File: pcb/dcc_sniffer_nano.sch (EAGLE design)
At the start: 8 parts, among them X1 RT034 Typ 086

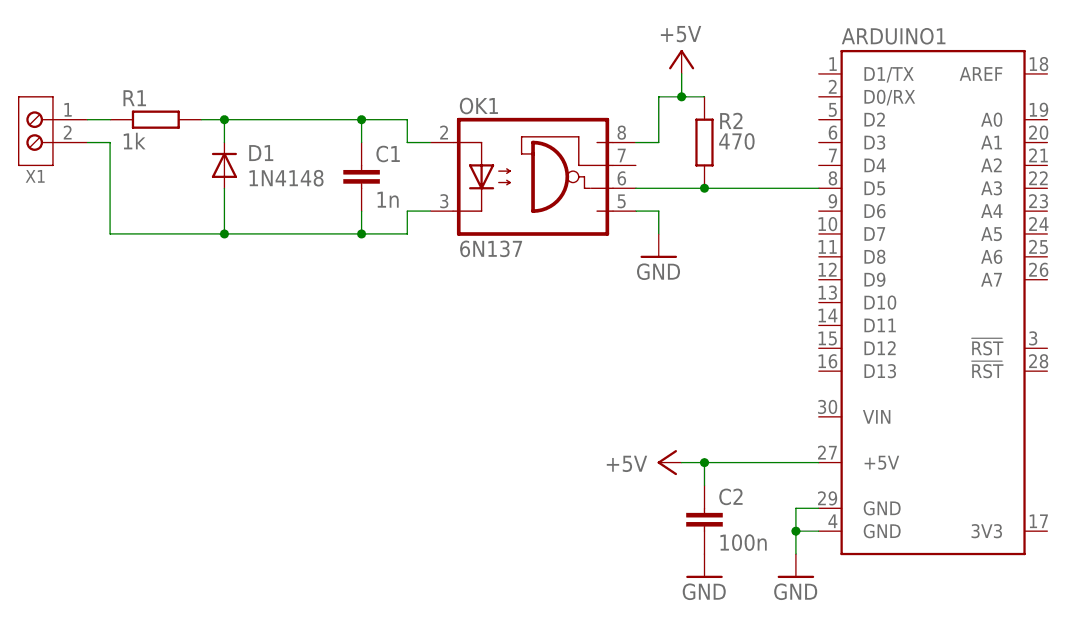
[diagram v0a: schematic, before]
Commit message: bugfix: assign to IRQ input pin
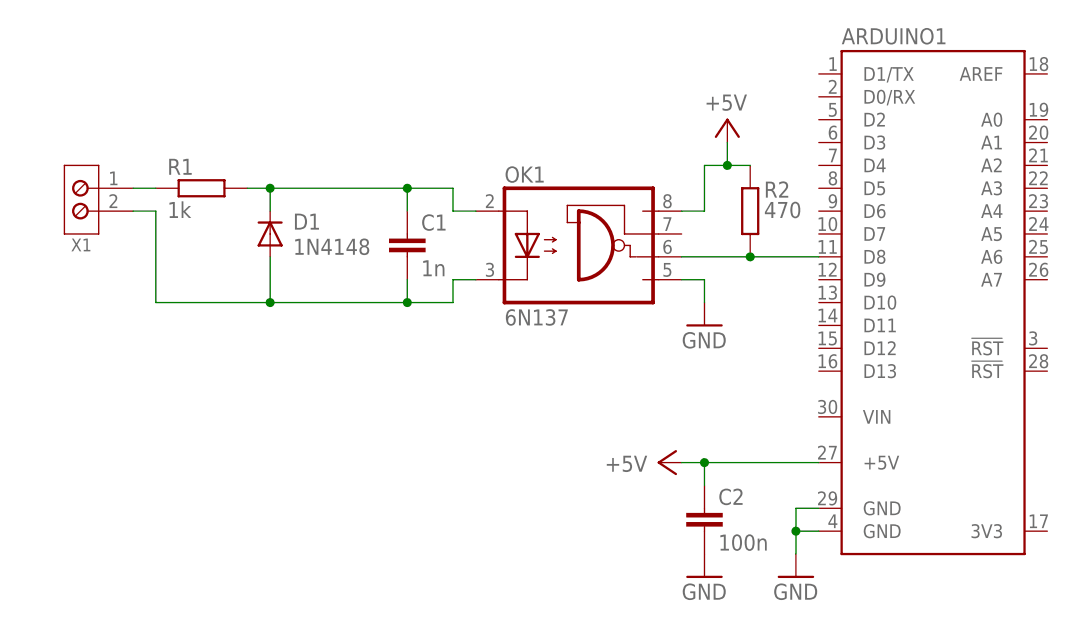
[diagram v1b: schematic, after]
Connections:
- net N$3: now also ARDUINO1.D8; no longer ARDUINO1.D5
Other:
- moved on the sheet: C1, D1, OK1, R1, R2, X1
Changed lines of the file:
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@@
 <sheet>
 <plain>
-<wire x1="30.48" y1="109.22" x2="34.29" y2="109.22" width="0.1524" layer="94"/>
-<wire x1="34.29" y1="109.22" x2="34.29" y2="116.84" width="0.1524" layer="94"/>
-<wire x1="34.29" y1="116.84" x2="30.48" y2="116.84" width="0.1524" layer="94"/>
-<wire x1="30.48" y1="116.84" x2="30.48" y2="109.22" width="0.1524" layer="94"/>
-<text x="29.718" y="108.458" size="1.4224" layer="98" font="vector" ratio="15" rot="R90">to track</text>
+<wire x1="35.56" y1="101.6" x2="39.37" y2="101.6" width="0.1524" layer="94"/>
+<wire x1="39.37" y1="101.6" x2="39.37" y2="109.22" width="0.1524" layer="94"/>
+<wire x1="39.37" y1="109.22" x2="35.56" y2="109.22" width="0.1524" layer="94"/>
+<wire x1="35.56" y1="109.22" x2="35.56" y2="101.6" width="0.1524" layer="94"/>
+<text x="34.798" y="100.838" size="1.4224" layer="98" font="vector" ratio="15" rot="R90">to track</text>
 </plain>
 <instances>
 <instance part="FRAME1" gate="G$1" x="0" y="0"/>
 <instance part="GND1" gate="1" x="116.84" y="63.5"/>
-<instance part="OK1" gate="A" x="88.9" y="106.68"/>
-<instance part="X1" gate="G$1" x="33.02" y="114.3" smashed="yes">
-<attribute name="PART" x="33.528" y="108.712" size="1.4224" layer="95" rot="R180"/>
+<instance part="OK1" gate="A" x="93.98" y="99.06"/>
+<instance part="X1" gate="G$1" x="38.1" y="106.68" smashed="yes">
+<attribute name="PART" x="38.608" y="101.092" size="1.4224" layer="95" rot="R180"/>
 </instance>
-<instance part="X1" gate="G$2" x="33.02" y="111.76" smashed="yes"/>
+<instance part="X1" gate="G$2" x="38.1" y="104.14" smashed="yes"/>
 <instance part="P+1" gate="1" x="101.6" y="76.2" smashed="yes" rot="R90">
 <attribute name="VALUE" x="100.33" y="76.962" size="1.778" layer="96" rot="R180"/>
 </instance>
-<instance part="D1" gate="G$1" x="53.34" y="109.22" smashed="yes" rot="R90">
-<attribute name="NAME" x="55.88" y="109.7026" size="1.778" layer="95"/>
-<attribute name="VALUE" x="55.88" y="106.9086" size="1.778" layer="96"/>
+<instance part="D1" gate="G$1" x="58.42" y="101.6" smashed="yes" rot="R90">
+<attribute name="NAME" x="60.96" y="102.0826" size="1.778" layer="95"/>
+<attribute name="VALUE" x="60.96" y="99.2886" size="1.778" layer="96"/>
 </instance>
-<instance part="R1" gate="G$1" x="45.72" y="114.3"/>
-<instance part="GND2" gate="1" x="101.6" y="99.06"/>
-<instance part="P+2" gate="1" x="104.14" y="121.92" smashed="yes">
-<attribute name="VALUE" x="101.6" y="122.936" size="1.778" layer="96"/>
+<instance part="R1" gate="G$1" x="50.8" y="106.68"/>
+<instance part="GND2" gate="1" x="106.68" y="91.44"/>
+<instance part="P+2" gate="1" x="109.22" y="114.3" smashed="yes">
+<attribute name="VALUE" x="106.68" y="115.316" size="1.778" layer="96"/>
 </instance>
-<instance part="R2" gate="G$1" x="106.68" y="111.76" smashed="yes" rot="R90">
-<attribute name="NAME" x="108.204" y="113.2586" size="1.778" layer="95"/>
-<attribute name="VALUE" x="108.204" y="110.998" size="1.778" layer="96"/>
+<instance part="R2" gate="G$1" x="111.76" y="104.14" smashed="yes" rot="R90">
+<attribute name="NAME" x="113.284" y="105.6386" size="1.778" layer="95"/>
+<attribute name="VALUE" x="113.284" y="103.378" size="1.778" layer="96"/>
 </instance>
 <instance part="ARDUINO1" gate="G$1" x="132.08" y="93.98"/>
-<instance part="C1" gate="G$1" x="68.58" y="109.22"/>
+<instance part="C1" gate="G$1" x="73.66" y="101.6"/>
 <instance part="C2" gate="G$1" x="106.68" y="71.12"/>
 <instance part="GND3" gate="1" x="106.68" y="63.5"/>
@@
 <segment>
 <pinref part="OK1" gate="A" pin="GND"/>
-<wire x1="99.06" y1="104.14" x2="101.6" y2="104.14" width="0.1524" layer="91"/>
+<wire x1="104.14" y1="96.52" x2="106.68" y2="96.52" width="0.1524" layer="91"/>
 <pinref part="GND2" gate="1" pin="GND"/>
-<wire x1="101.6" y1="104.14" x2="101.6" y2="101.6" width="0.1524" layer="91"/>
+<wire x1="106.68" y1="96.52" x2="106.68" y2="93.98" width="0.1524" layer="91"/>
 </segment>
 <segment>
@@
 <segment>
 <pinref part="OK1" gate="A" pin="VCC"/>
-<wire x1="99.06" y1="111.76" x2="101.6" y2="111.76" width="0.1524" layer="91"/>
-<wire x1="101.6" y1="111.76" x2="101.6" y2="116.84" width="0.1524" layer="91"/>
+<wire x1="104.14" y1="104.14" x2="106.68" y2="104.14" width="0.1524" layer="91"/>
+<wire x1="106.68" y1="104.14" x2="106.68" y2="109.22" width="0.1524" layer="91"/>
 <pinref part="R2" gate="G$1" pin="2"/>
-<wire x1="106.68" y1="116.84" x2="104.14" y2="116.84" width="0.1524" layer="91"/>
+<wire x1="111.76" y1="109.22" x2="109.22" y2="109.22" width="0.1524" layer="91"/>
 <pinref part="P+2" gate="1" pin="+5V"/>
-<wire x1="104.14" y1="116.84" x2="101.6" y2="116.84" width="0.1524" layer="91"/>
-<wire x1="104.14" y1="119.38" x2="104.14" y2="116.84" width="0.1524" layer="91"/>
-<junction x="104.14" y="116.84"/>
+<wire x1="109.22" y1="109.22" x2="106.68" y2="109.22" width="0.1524" layer="91"/>
+<wire x1="109.22" y1="111.76" x2="109.22" y2="109.22" width="0.1524" layer="91"/>
+<junction x="109.22" y="109.22"/>
 </segment>
 </net>
@@
 <segment>
 <pinref part="OK1" gate="A" pin="A"/>
-<wire x1="76.2" y1="111.76" x2="73.66" y2="111.76" width="0.1524" layer="91"/>
-<wire x1="73.66" y1="111.76" x2="73.66" y2="114.3" width="0.1524" layer="91"/>
-<wire x1="73.66" y1="114.3" x2="68.58" y2="114.3" width="0.1524" layer="91"/>
-<wire x1="68.58" y1="114.3" x2="53.34" y2="114.3" width="0.1524" layer="91"/>
-<wire x1="68.58" y1="111.76" x2="68.58" y2="114.3" width="0.1524" layer="91"/>
-<junction x="68.58" y="114.3"/>
+<wire x1="81.28" y1="104.14" x2="78.74" y2="104.14" width="0.1524" layer="91"/>
+<wire x1="78.74" y1="104.14" x2="78.74" y2="106.68" width="0.1524" layer="91"/>
+<wire x1="78.74" y1="106.68" x2="73.66" y2="106.68" width="0.1524" layer="91"/>
+<wire x1="73.66" y1="106.68" x2="58.42" y2="106.68" width="0.1524" layer="91"/>
+<wire x1="73.66" y1="104.14" x2="73.66" y2="106.68" width="0.1524" layer="91"/>
+<junction x="73.66" y="106.68"/>
 <pinref part="D1" gate="G$1" pin="C"/>
-<wire x1="53.34" y1="114.3" x2="53.34" y2="111.76" width="0.1524" layer="91"/>
+<wire x1="58.42" y1="106.68" x2="58.42" y2="104.14" width="0.1524" layer="91"/>
 <pinref part="R1" gate="G$1" pin="2"/>
-<wire x1="53.34" y1="114.3" x2="50.8" y2="114.3" width="0.1524" layer="91"/>
-<junction x="53.34" y="114.3"/>
+<wire x1="58.42" y1="106.68" x2="55.88" y2="106.68" width="0.1524" layer="91"/>
+<junction x="58.42" y="106.68"/>
 <pinref part="C1" gate="G$1" pin="1"/>
 </segment>
@@
 <segment>
 <pinref part="OK1" gate="A" pin="C"/>
-<wire x1="76.2" y1="104.14" x2="73.66" y2="104.14" width="0.1524" layer="91"/>
-<wire x1="73.66" y1="104.14" x2="73.66" y2="101.6" width="0.1524" layer="91"/>
-<wire x1="73.66" y1="101.6" x2="68.58" y2="101.6" width="0.1524" layer="91"/>
-<wire x1="68.58" y1="101.6" x2="53.34" y2="101.6" width="0.1524" layer="91"/>
-<wire x1="68.58" y1="104.14" x2="68.58" y2="101.6" width="0.1524" layer="91"/>
-<junction x="68.58" y="101.6"/>
+<wire x1="81.28" y1="96.52" x2="78.74" y2="96.52" width="0.1524" layer="91"/>
+<wire x1="78.74" y1="96.52" x2="78.74" y2="93.98" width="0.1524" layer="91"/>
+<wire x1="78.74" y1="93.98" x2="73.66" y2="93.98" width="0.1524" layer="91"/>
+<wire x1="73.66" y1="93.98" x2="58.42" y2="93.98" width="0.1524" layer="91"/>
+<wire x1="73.66" y1="96.52" x2="73.66" y2="93.98" width="0.1524" layer="91"/>
+<junction x="73.66" y="93.98"/>
 <pinref part="D1" gate="G$1" pin="A"/>
-<wire x1="53.34" y1="101.6" x2="53.34" y2="106.68" width="0.1524" layer="91"/>
+<wire x1="58.42" y1="93.98" x2="58.42" y2="99.06" width="0.1524" layer="91"/>
 <pinref part="X1" gate="G$2" pin="P$1"/>
-<wire x1="38.1" y1="111.76" x2="40.64" y2="111.76" width="0.1524" layer="91"/>
-<wire x1="40.64" y1="111.76" x2="40.64" y2="101.6" width="0.1524" layer="91"/>
-<wire x1="40.64" y1="101.6" x2="53.34" y2="101.6" width="0.1524" layer="91"/>
-<junction x="53.34" y="101.6"/>
+<wire x1="43.18" y1="104.14" x2="45.72" y2="104.14" width="0.1524" layer="91"/>
+<wire x1="45.72" y1="104.14" x2="45.72" y2="93.98" width="0.1524" layer="91"/>
+<wire x1="45.72" y1="93.98" x2="58.42" y2="93.98" width="0.1524" layer="91"/>
+<junction x="58.42" y="93.98"/>
 <pinref part="C1" gate="G$1" pin="2"/>
 </segment>
@@
 <segment>
 <pinref part="OK1" gate="A" pin="VO"/>
-<wire x1="99.06" y1="106.68" x2="106.68" y2="106.68" width="0.1524" layer="91"/>
+<wire x1="104.14" y1="99.06" x2="111.76" y2="99.06" width="0.1524" layer="91"/>
 <pinref part="R2" gate="G$1" pin="1"/>
-<wire x1="119.38" y1="106.68" x2="106.68" y2="106.68" width="0.1524" layer="91"/>
-<junction x="106.68" y="106.68"/>
-<pinref part="ARDUINO1" gate="G$1" pin="D5"/>
+<junction x="111.76" y="99.06"/>
+<pinref part="ARDUINO1" gate="G$1" pin="D8"/>
+<wire x1="119.38" y1="99.06" x2="111.76" y2="99.06" width="0.1524" layer="91"/>
 </segment>
 </net>
@@
 <pinref part="R1" gate="G$1" pin="1"/>
 <pinref part="X1" gate="G$1" pin="P$1"/>
-<wire x1="40.64" y1="114.3" x2="38.1" y2="114.3" width="0.1524" layer="91"/>
+<wire x1="45.72" y1="106.68" x2="43.18" y2="106.68" width="0.1524" layer="91"/>
 </segment>
 </net>
